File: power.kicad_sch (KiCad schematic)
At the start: 70 parts, among them J2 Molex_Mini-Fit_2x3_50362462, Q16 DMG1012T-7, Q2 SISS05DN-T1-GE3, Q23 SISS05DN-T1-GE3, Q24 SISS05DN-T1-GE3, Q25 SISS05DN-T1-GE3, Q4 DMG1012T-7, Q5 SISS05DN-T1-GE3, Q6 DMG1012T-7, Q9 SISS05DN-T1-GE3, U15 NCP730BMT330_WSON, U6 LTC4412IS6, U61 LTC4412IS6, U62 LTC4412IS6, U63 LTC4412IS6, U64 LTC4412IS6

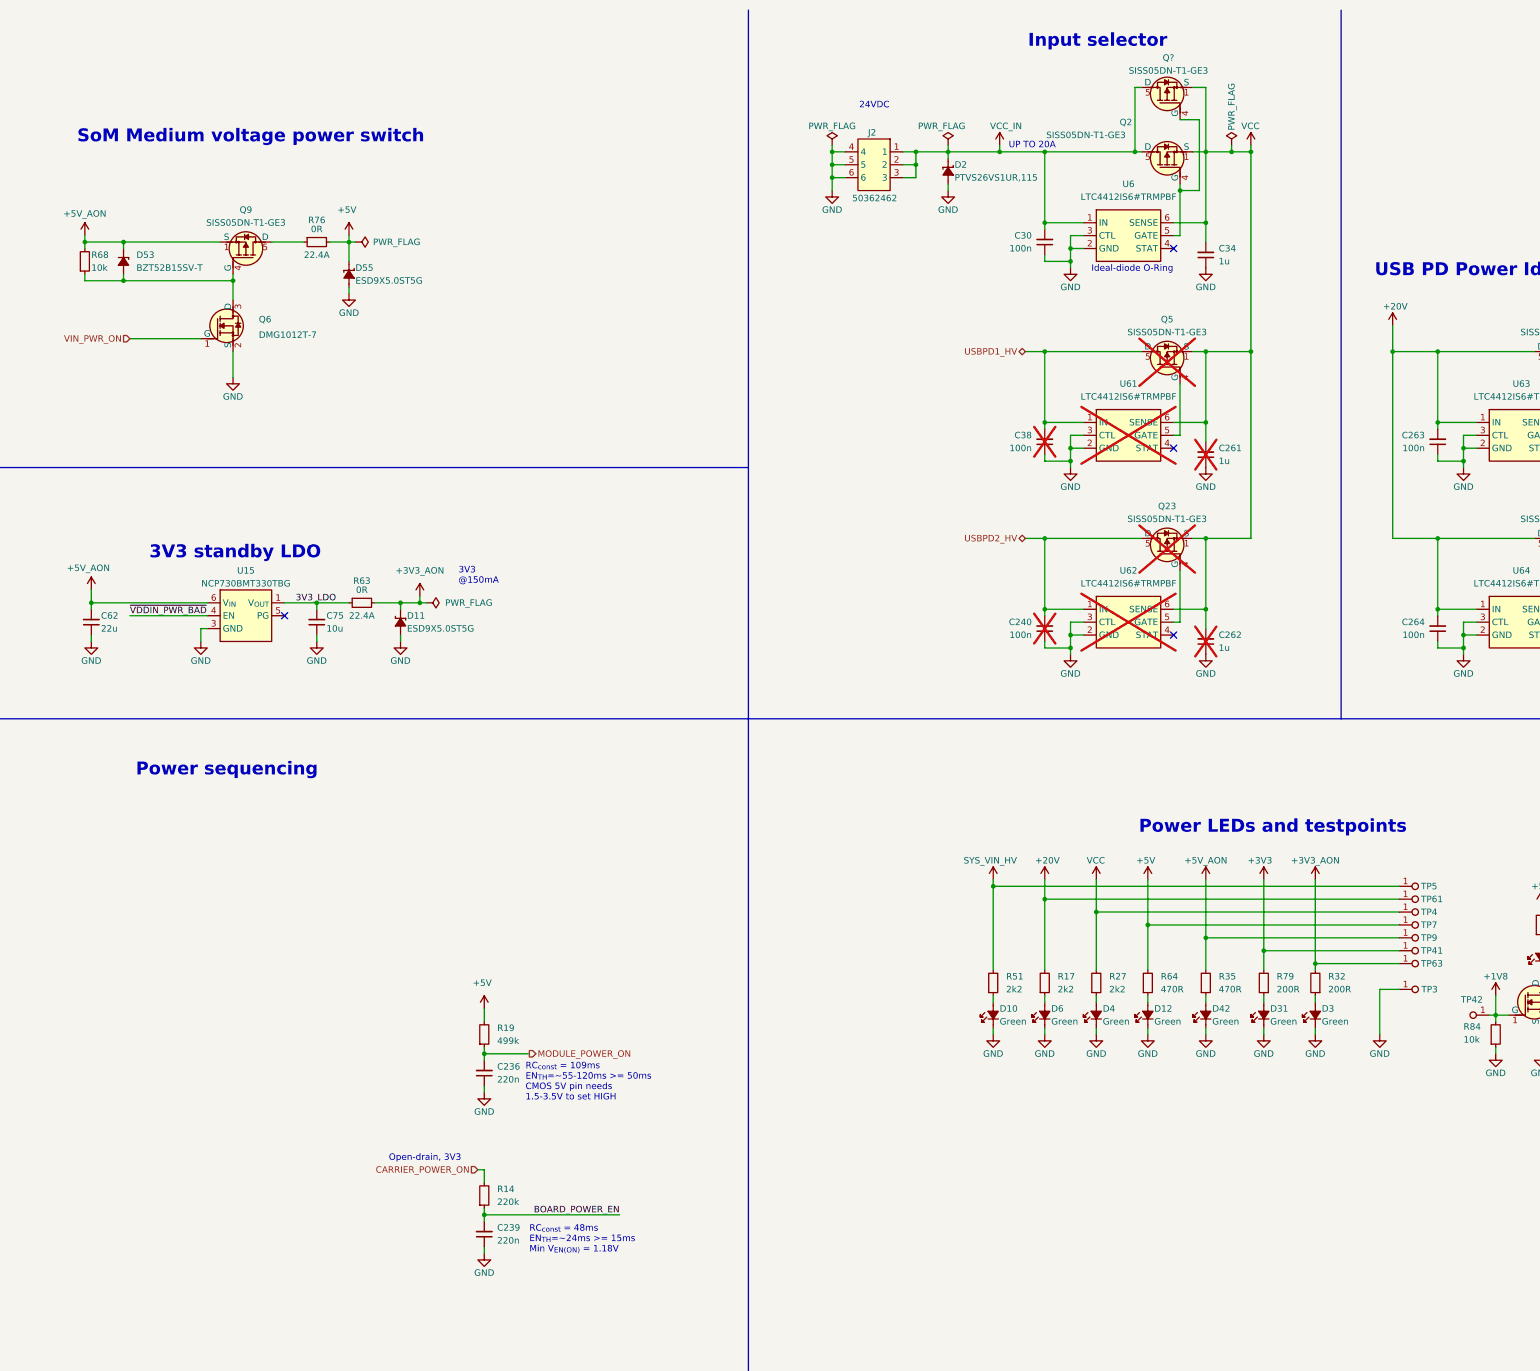
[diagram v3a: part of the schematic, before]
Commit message: [#85488] Correct Power sequence
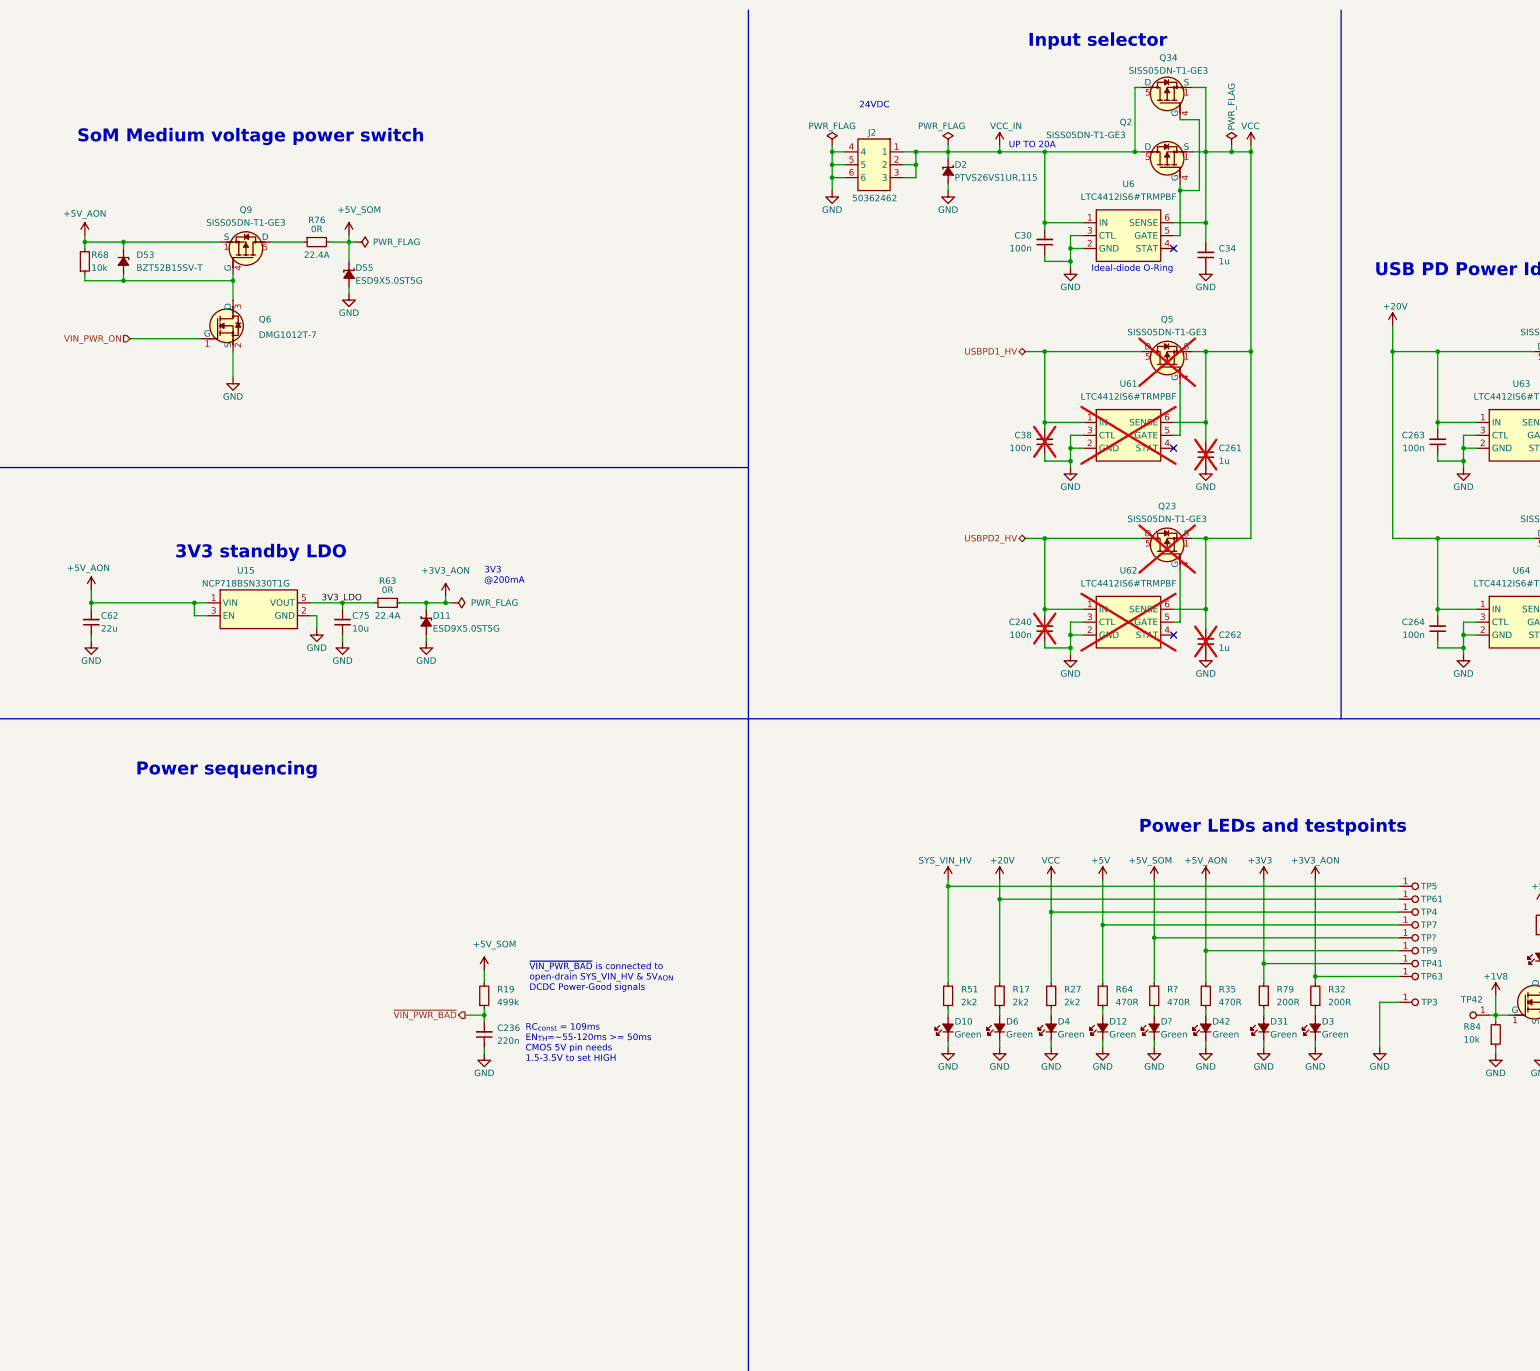
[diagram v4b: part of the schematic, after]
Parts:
- removed C239: C_220n_0402, antmicro-footprints:C_0402_1005Metric, symbol antmicroCapacitors0402:C_220n_0402
- removed R14: R_220k_0402, antmicro-footprints:R_0402_1005Metric, symbol antmicroResistors0402:R_220k_0402
- added D?: LED_G_0603_LTST-C190GKT, antmicro-footprints:LED_0603_1608Metric_G, symbol antmicroLEDIndicationDiscrete:LED_G_0603_LTST-C190GKT
- added R?: R_470R_0402, antmicro-footprints:R_0402_1005Metric, symbol antmicroResistors0402:R_470R_0402
- added TP?: TP_0.75mm_SMD, antmicro-footprints:TP_SMD_0.75mm, symbol antmicroTestPoints:TP_0.75mm_SMD
- U15: value NCP730BMT330_WSON -> NCP718BSN330T1G; footprint antmicro-footprints:WSON-6-1EP_2x2mm_P0.65mm -> antmicro-footprints:SOT-23-5; symbol antmicroPMICVoltageRegulatorsLinear:NCP730BMT330_WSON -> antmicroPMICVoltageRegulatorsLinear:NCP718BSN330T1G; MPN NCP730BMT330TBG -> NCP718BSN330T1G
- gave numbers to parts that had none: 1
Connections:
- net +5V: no longer D55.1 (C), R19.2, R76.2
- net +5V_AON: now also U15.1 (VIN), U15.3 (EN); no longer U15.6 (V_{IN})
- net 3V3_LDO: now also U15.5 (VOUT); no longer U15.1 (V_{OUT})
- net GND: now also U15.2 (GND), D?.1 (C); no longer U15.3 (GND), U15.7 (GND)
- net MODULE_POWER_ON renamed ~{VIN_PWR_BAD}
- net ~{VDDIN_PWR_BAD}: no longer names the net of U15.4 (NC)
- new net: D?.2 (A), R?.1
- new net +5V_SOM: D55.1 (C), R19.2, R76.2, R?.2, TP?.1
- no-connect marks 6 -> 5
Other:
- note added: "3V3 @200mA"
- note added: "~{VIN_PWR_BAD} is connected to open-drain SYS_VIN_HV & 5V_{AON} DCDC Power-Good signals"
- note removed: "3V3 @150mA"
- note removed: "Open-drain, 3V3"
- note removed: "RC_{const} = 48ms EN_{TH}=~24ms >= 15ms Min V_{EN(ON)} = 1.18V"
- moved on the sheet: C236, C75, D10, D11, D12, D3, D31, D4, D42, D6, R17, R19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

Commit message: [#85488] Sync sch branches
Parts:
- gave numbers to parts that had none: 3
- renumbered Q34 to Q39
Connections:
- net ~{VIN_PWR_BAD} renamed ~{VDDIN_PWR_BAD}
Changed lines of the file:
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@@
 		)
 	)
-	(hierarchical_label "~{VIN_PWR_BAD}"
+	(hierarchical_label "~{VDDIN_PWR_BAD}"
 		(shape output)
 		(at 133.35 210.82 180)
@@
 		(on_board yes)
 		(dnp no)
-		(property "Reference" "D?"
+		(property "Reference" "D61"
 			(at 270.51 212.09 90)
 			(effects
@@
 			(project "jetson-agx-thor-baseboard"
 				(path "/f569b0be-0afd-48b7-93ee-28582a4c645c/18ddd5dc-52e2-402c-b2e2-8bb33f110eab"
-					(reference "D?")
+					(reference "D61")
 					(unit 1)
 				)
@@
 		(on_board yes)
 		(dnp no)
-		(property "Reference" "Q34"
+		(property "Reference" "Q39"
 			(at 272.034 22.098 90)
 			(effects
@@
 			(project "jetson-agx-thor-baseboard"
 				(path "/f569b0be-0afd-48b7-93ee-28582a4c645c/18ddd5dc-52e2-402c-b2e2-8bb33f110eab"
-					(reference "Q34")
+					(reference "Q39")
 					(unit 1)
 				)
@@
 		(dnp no)
 		(fields_autoplaced yes)
-		(property "Reference" "R?"
+		(property "Reference" "R61"
 			(at 271.78 205.74 90)
 			(effects
@@
 			(project "jetson-agx-thor-baseboard"
 				(path "/f569b0be-0afd-48b7-93ee-28582a4c645c/18ddd5dc-52e2-402c-b2e2-8bb33f110eab"
-					(reference "R?")
+					(reference "R61")
 					(unit 1)
 				)
@@
 		(on_board yes)
 		(dnp no)
-		(property "Reference" "TP?"
+		(property "Reference" "TP75"
 			(at 321.818 195.58 0)
 			(effects
@@
 			(project "jetson-agx-thor-baseboard"
 				(path "/f569b0be-0afd-48b7-93ee-28582a4c645c/18ddd5dc-52e2-402c-b2e2-8bb33f110eab"
-					(reference "TP?")
+					(reference "TP75")
 					(unit 1)
 				)

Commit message: [#85488] Annotate sch
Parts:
- C236: symbol antmicroCapacitors0402:C_220n_0402 -> antmicroCapacitors0402:C_100n_0402; Dielectric (none) -> X5R; MPN CC0402KRX5R6BB224 -> GRM155R61H104KE14D; Manufacturer YAGEO -> Murata; Val 220n -> 100n; Voltage (none) -> 50V
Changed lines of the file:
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@@
 	(title_block
 		(title "Jetson AGX Thor Baseboard")
-		(date "2025-10-16")
+		(date "2025-10-21")
 		(rev "1.0.0")
 		(company "Antmicro Ltd")
@@
 	)
 	(symbol
-		(lib_id "antmicroCapacitors0402:C_220n_0402")
+		(lib_id "antmicroCapacitors0402:C_100n_0402")
 		(at 137.16 217.17 90)
 		(unit 1)
@@
 			)
 		)
-		(property "Datasheet" "https://www.yageo.com/en/Chart/Download/pdf/CC0402KRX5R6BB224"
+		(property "Datasheet" "https://www.murata.com/products/productdetail?partno=GRM155R61H104KE14%23"
 			(at 152.4 196.85 0)
 			(effects
@@
 			)
 		)
-		(property "Description" "SMD Multilayer Ceramic Capacitor, 0.22 µF, 10 V, 0402 [1005 Metric], ± 10%, X5R, CC Series"
+		(property "Description" "SMD Multilayer Ceramic Capacitor, 0.1 µF, 50 V, 0402 [1005 Metric], ± 10%, X5R, GRM Series"
 			(at 170.18 196.85 0)
 			(effects
@@
 			)
 		)
-		(property "MPN" "CC0402KRX5R6BB224"
+		(property "MPN" "GRM155R61H104KE14D"
 			(at 154.94 196.85 0)
 			(effects
@@
 			)
 		)
-		(property "Manufacturer" "YAGEO"
+		(property "Manufacturer" "Murata"
 			(at 157.48 196.85 0)
 			(effects
@@
 			)
 		)
-		(property "Val" "220n"
+		(property "Val" "100n"
 			(at 139.7 215.8936 90)
 			(effects
@@
 			)
 		)
-		(property "Voltage" ""
+		(property "Voltage" "50V"
 			(at 165.1 196.85 0)
 			(effects
@@
 			)
 		)
-		(property "Dielectric" ""
+		(property "Dielectric" "X5R"
 			(at 167.64 196.85 0)
 			(effects

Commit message: [#85326] Clean DRC
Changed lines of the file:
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@@
 	)
 	(junction
-		(at 205.74 43.18)
+		(at 207.01 43.18)
 		(diameter 0)
 		(color 0 0 0 0)
@@
 	)
 	(junction
-		(at 205.74 40.64)
+		(at 207.01 40.64)
 		(diameter 0)
 		(color 0 0 0 0)
@@
 	)
 	(junction
-		(at 205.74 45.72)
+		(at 207.01 45.72)
 		(diameter 0)
 		(color 0 0 0 0)
@@
 	(wire
 		(pts
-			(xy 208.28 40.64) (xy 205.74 40.64)
+			(xy 209.55 40.64) (xy 207.01 40.64)
 		)
 		(stroke
@@
 	(wire
 		(pts
+			(xy 247.65 78.74) (xy 247.65 80.01)
+		)
+		(stroke
+			(width 0)
+			(type default)
+		)
+	)
+	(wire
+		(pts
 			(xy 313.69 208.28) (xy 313.69 217.17)
 		)
@@
 	(wire
 		(pts
-			(xy 205.74 45.72) (xy 205.74 48.26)
+			(xy 207.01 45.72) (xy 207.01 48.26)
 		)
 		(stroke
@@
 	(wire
 		(pts
-			(xy 208.28 45.72) (xy 205.74 45.72)
+			(xy 209.55 45.72) (xy 207.01 45.72)
 		)
 		(stroke
@@
 	(wire
 		(pts
-			(xy 208.28 43.18) (xy 205.74 43.18)
+			(xy 209.55 43.18) (xy 207.01 43.18)
 		)
 		(stroke
@@
 	(wire
 		(pts
+			(xy 247.65 115.57) (xy 247.65 116.84)
+		)
+		(stroke
+			(width 0)
+			(type default)
+		)
+	)
+	(wire
+		(pts
 			(xy 368.3 210.82) (xy 368.3 212.09)
 		)
@@
 	(wire
 		(pts
-			(xy 205.74 40.64) (xy 205.74 43.18)
+			(xy 207.01 40.64) (xy 207.01 43.18)
 		)
 		(stroke
@@
 	(wire
 		(pts
-			(xy 205.74 43.18) (xy 205.74 45.72)
+			(xy 207.01 43.18) (xy 207.01 45.72)
 		)
 		(stroke
@@
 	(wire
 		(pts
-			(xy 205.74 39.37) (xy 205.74 40.64)
+			(xy 207.01 39.37) (xy 207.01 40.64)
 		)
 		(stroke
@@
 			)
 		)
-		(property "Description" "Pin Header, Wire-to-Board, 2 Rows, 6 Contacts, Through Hole Right-Angle, Mini-Fit"
+		(property "Description" "Pin Header, Wire-to-Board, 2 Rows, 6 Contacts, Through Hole Right-Angle, Mini-Fit, 13A/pin, 600V, 4.2mm"
 			(at 190.5 63.5 0)
 			(effects
@@
 	(symbol
 		(lib_id "antmicropower:PWR_FLAG")
-		(at 205.74 39.37 0)
+		(at 207.01 39.37 0)
 		(mirror y)
 		(unit 1)
@@
 		(dnp no)
 		(property "Reference" "#FLG012"
-			(at 205.74 37.465 0)
+			(at 207.01 37.465 0)
 			(effects
 				(font
@@
 		)
 		(property "Value" "PWR_FLAG"
-			(at 205.74 35.56 0)
+			(at 207.01 35.56 0)
 			(effects
 				(font
@@
 		)
 		(property "Footprint" ""
-			(at 205.74 39.37 0)
+			(at 207.01 39.37 0)
 			(effects
 				(font
@@
 		)
 		(property "Datasheet" ""
-			(at 205.74 39.37 0)
+			(at 207.01 39.37 0)
 			(effects
 				(font
@@
 		)
 		(property "Description" ""
-			(at 205.74 39.37 0)
+			(at 207.01 39.37 0)
 			(effects
 				(font
@@
 	(symbol
 		(lib_id "antmicropower:GND")
-		(at 205.74 48.26 0)
+		(at 207.01 48.26 0)
 		(mirror y)
 		(unit 1)
@@
 		(dnp no)
 		(property "Reference" "#PWR079"
-			(at 205.74 54.61 0)
+			(at 207.01 54.61 0)
 			(effects
 				(font
@@
 		)
 		(property "Value" "GND"
-			(at 205.74 52.07 0)
+			(at 207.01 52.07 0)
 			(effects
 				(font
@@
 		)
 		(property "Footprint" ""
-			(at 196.85 55.88 0)
+			(at 198.12 55.88 0)
 			(effects
 				(font
@@
 		)
 		(property "Datasheet" ""
-			(at 196.85 60.96 0)
+			(at 198.12 60.96 0)
 			(effects
 				(font
@@
 		)
 		(property "Description" ""
-			(at 205.74 48.26 0)
+			(at 207.01 48.26 0)
 			(effects
 				(font
@@
 		)
 		(property "Author" "Antmicro"
-			(at 196.85 55.88 0)
+			(at 198.12 55.88 0)
 			(effects
 				(font
@@
 		)
 		(property "License" "Apache-2.0"
-			(at 196.85 58.42 0)
+			(at 198.12 58.42 0)
 			(effects
 				(font
@@
 	)
 	(symbol
+		(lib_id "antmicropower:PWR_FLAG")
+		(at 247.65 78.74 0)
+		(unit 1)
+		(exclude_from_sim no)
+		(in_bom yes)
+		(on_board yes)
+		(dnp no)
+		(property "Reference" "#FLG08"
+			(at 247.65 76.835 0)
+			(effects
+				(font
+					(size 1.27 1.27)
+				)
+				(hide yes)
+			)
+		)
+		(property "Value" "PWR_FLAG"
+			(at 247.65 74.93 0)
+			(effects
+				(font
+					(size 1.27 1.27)
+				)
+			)
+		)
+		(property "Footprint" ""
+			(at 247.65 78.74 0)
+			(effects
+				(font
+					(size 1.27 1.27)
+				)
+				(hide yes)
+			)
+		)
+		(property "Datasheet" ""
+			(at 247.65 78.74 0)
+			(effects
+				(font
+					(size 1.27 1.27)
+				)
+				(hide yes)
+			)
+		)
+		(property "Description" ""
+			(at 247.65 78.74 0)
+			(effects
+				(font
+					(size 1.27 1.27)
+				)
+				(hide yes)
+			)
+		)
+		(pin "1"
+		)
+		(instances
+			(project "jetson-agx-thor-baseboard"
+				(path "/f569b0be-0afd-48b7-93ee-28582a4c645c/18ddd5dc-52e2-402c-b2e2-8bb33f110eab"
+					(reference "#FLG08")
+					(unit 1)
+				)
+			)
+		)
+	)
+	(symbol
 		(lib_id "antmicropower:VCC")
 		(at 228.6 184.15 0)
@@
 					(unit 1)
 				)
+			)
+		)
+	)
+	(symbol
+		(lib_id "antmicropower:PWR_FLAG")
+		(at 247.65 115.57 0)
+		(unit 1)
+		(exclude_from_sim no)
+		(in_bom yes)
+		(on_board yes)
+		(dnp no)
+		(property "Reference" "#FLG013"
+			(at 247.65 113.665 0)
+			(effects
+				(font
+					(size 1.27 1.27)
+				)
+				(hide yes)
+			)
+		)
+		(property "Value" "PWR_FLAG"
+			(at 247.65 111.76 0)
+			(effects
+				(font
+					(size 1.27 1.27)
+				)
+			)
+		)
+		(property "Footprint" ""
+			(at 247.65 115.57 0)
+			(effects
+				(font
+					(size 1.27 1.27)
+				)
+				(hide yes)
+			)
+		)
+		(property "Datasheet" ""
+			(at 247.65 115.57 0)
+			(effects
+				(font
+					(size 1.27 1.27)
+				)
+				(hide yes)
+			)
+		)
+		(property "Description" ""
+			(at 247.65 115.57 0)
+			(effects
+				(font
+					(size 1.27 1.27)
+				)
+				(hide yes)
+			)
+		)
+		(pin "1"
+		)
+		(instances
+			(project "jetson-agx-thor-baseboard"
+				(path "/f569b0be-0afd-48b7-93ee-28582a4c645c/18ddd5dc-52e2-402c-b2e2-8bb33f110eab"
+					(reference "#FLG013")
+					(unit 1)
+				)
